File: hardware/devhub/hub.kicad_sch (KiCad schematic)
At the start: 34 parts, among them J2 USB-C UPSTREAM, J3 PORTA 7 (scorta), U12 MCP120T-300I/TT, U2 USB2517I-JZX, Y1 24MHz 12pF

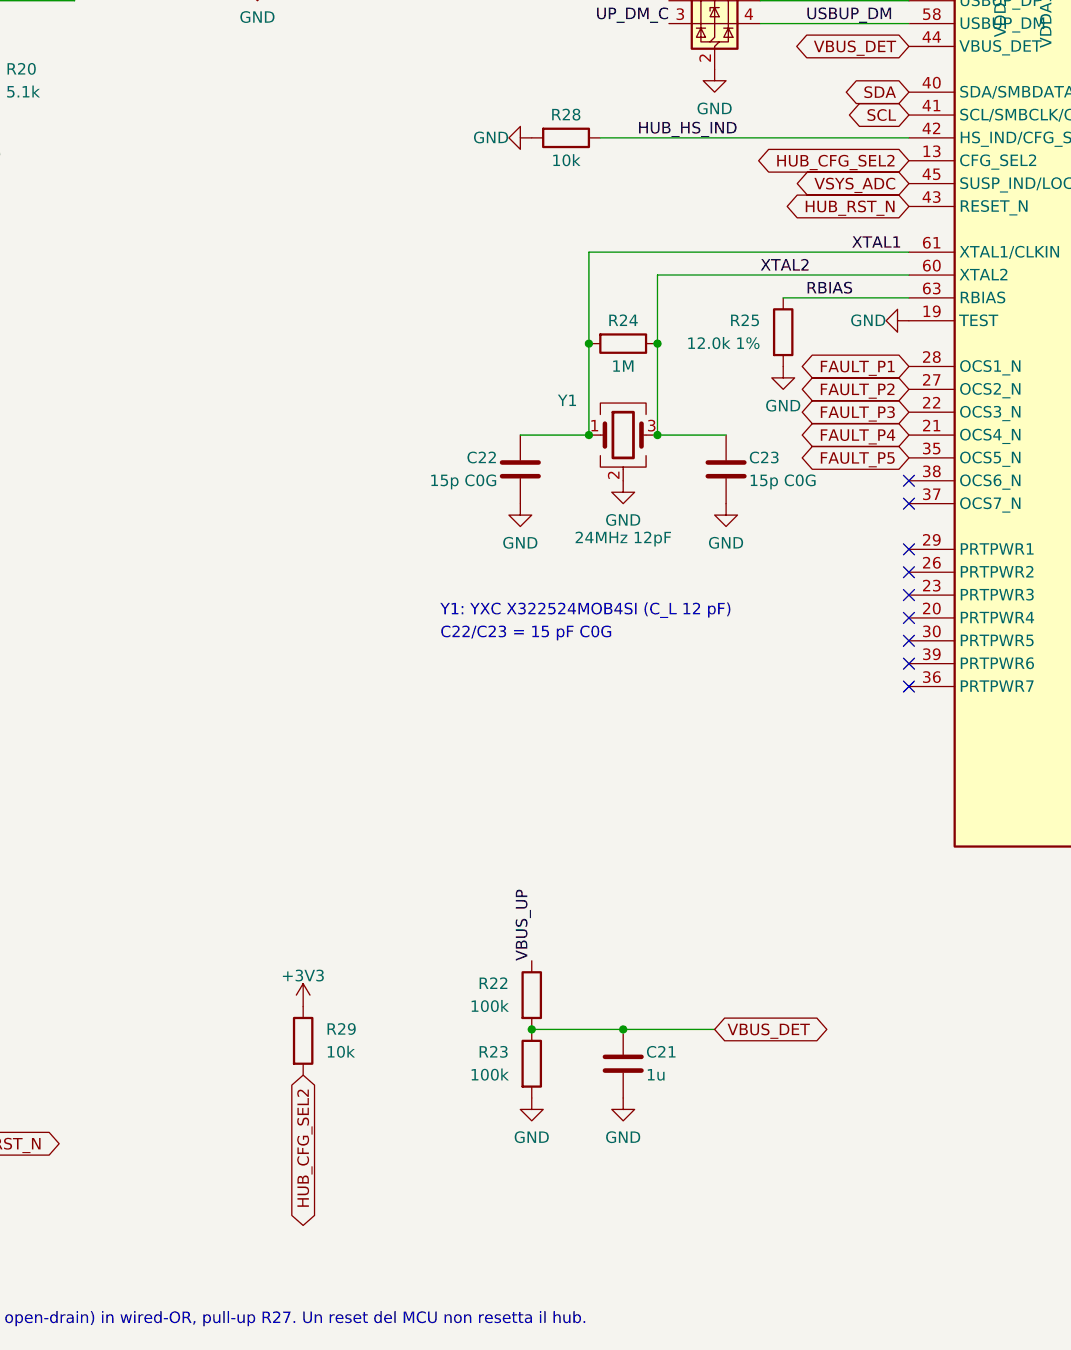
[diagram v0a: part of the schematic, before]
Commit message: Simplification: input shunt moved after the eFuse, VSYS_ADC divider removed (D40)
The INA3221 is no longer exposed to the supply voltage and reads 5V_SYS; LOCAL_PWR gets a 10k pull-up (R26). Push-button capacitors kept (D39).
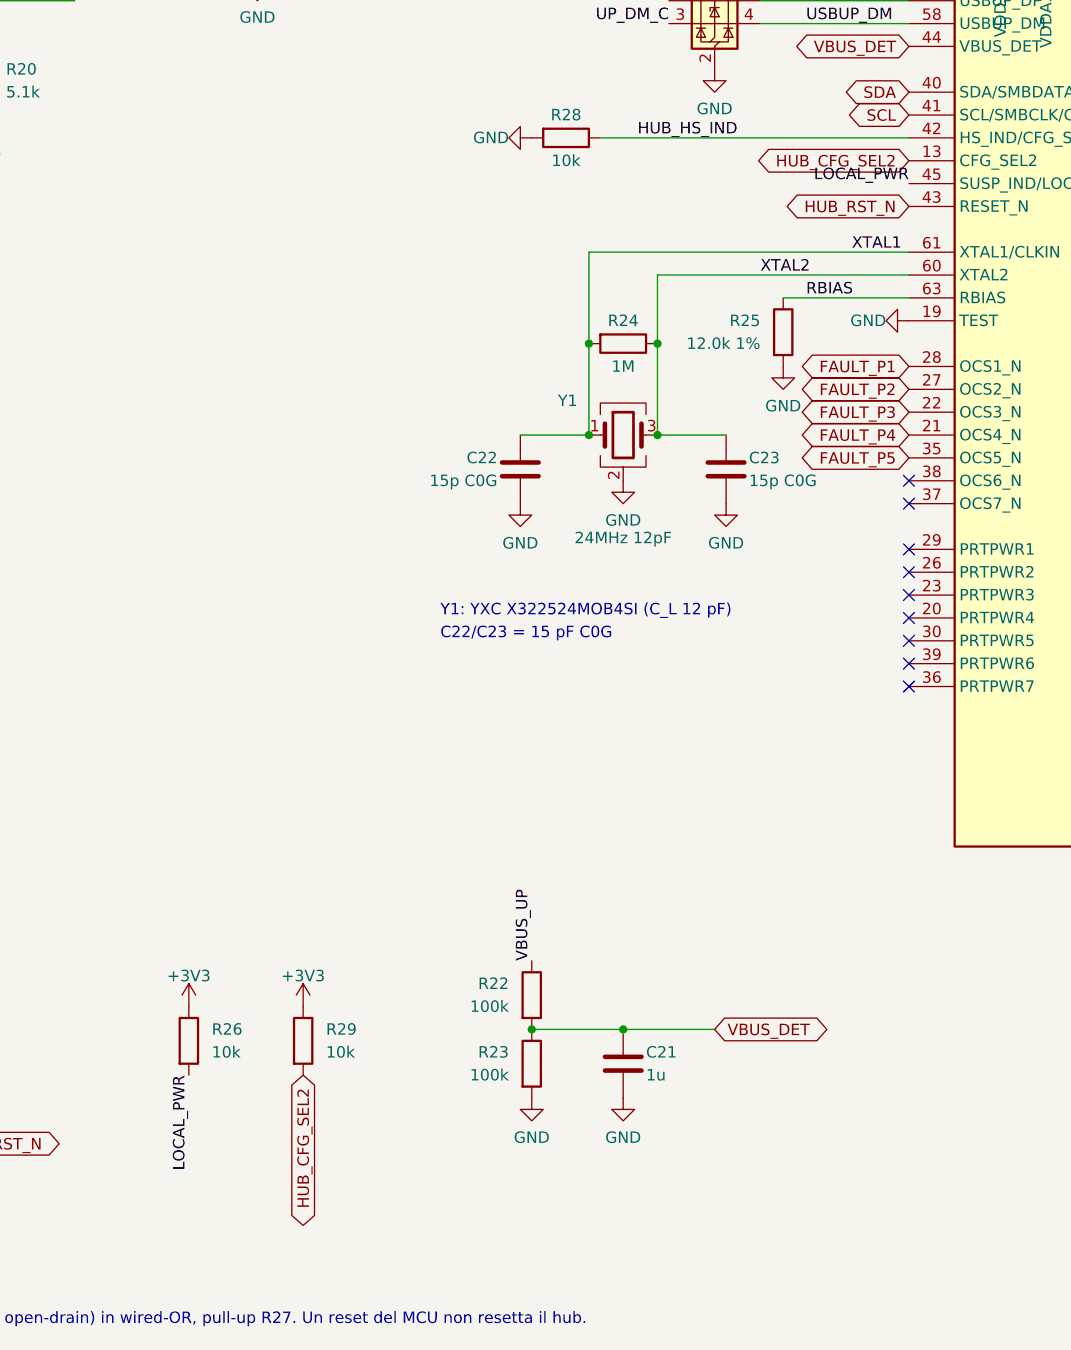
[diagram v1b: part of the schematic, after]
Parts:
- added R26: 10k, Resistor_SMD:R_0603_1608Metric, symbol Device:R
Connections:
- net +3V3: now also R26.1
- net VSYS_ADC renamed LOCAL_PWR
- net LOCAL_PWR: now also R26.2
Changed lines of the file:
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@@
 		)
 	)
+	(label "LOCAL_PWR"
+		(at 184.15 127 180)
+		(effects
+			(font
+				(size 1.27 1.27)
+			)
+			(justify right bottom)
+		)
+	)
+	(label "LOCAL_PWR"
+		(at 104.14 226.06 270)
+		(effects
+			(font
+				(size 1.27 1.27)
+			)
+			(justify right bottom)
+		)
+	)
 	(global_label "USB_MCU_DM"
 		(shape bidirectional)
@@
 		)
 	)
-	(global_label "VSYS_ADC"
-		(shape bidirectional)
-		(at 184.15 127 180)
-		(fields_autoplaced yes)
-		(effects
-			(font
-				(size 1.27 1.27)
-			)
-			(justify right)
-		)
-		(property "Intersheetrefs" "${INTERSHEET_REFS}"
-			(at 184.15 127 0)
-			(hide yes)
-			(show_name no)
-			(do_not_autoplace no)
-			(effects
-				(font
-					(size 1.27 1.27)
-				)
-			)
-		)
-	)
 	(symbol
 		(lib_id "Device:R")
@@
 					(unit 1)
 				)
+			)
+		)
+	)
+	(symbol
+		(lib_id "Device:R")
+		(at 104.14 222.25 0)
+		(unit 1)
+		(body_style 1)
+		(exclude_from_sim no)
+		(in_bom yes)
+		(on_board yes)
+		(in_pos_files yes)
+		(dnp no)
+		(property "Reference" "R26"
+			(at 106.68 220.98 0)
+			(show_name no)
+			(do_not_autoplace no)
+			(effects
+				(font
+					(size 1.27 1.27)
+				)
+				(justify left)
+			)
+		)
+		(property "Value" "10k"
+			(at 106.68 223.52 0)
+			(show_name no)
+			(do_not_autoplace no)
+			(effects
+				(font
+					(size 1.27 1.27)
+				)
+				(justify left)
+			)
+		)
+		(property "Footprint" "Resistor_SMD:R_0603_1608Metric"
+			(at 104.14 222.25 0)
+			(hide yes)
+			(show_name no)
+			(do_not_autoplace no)
+			(effects
+				(font
+					(size 1.27 1.27)
+				)
+			)
+		)
+		(property "Datasheet" ""
+			(at 104.14 222.25 0)
+			(hide yes)
+			(show_name no)
+			(do_not_autoplace no)
+			(effects
+				(font
+					(size 1.27 1.27)
+				)
+			)
+		)
+		(property "Description" "Resistor"
+			(at 104.14 222.25 0)
+			(hide yes)
+			(show_name no)
+			(do_not_autoplace no)
+			(effects
+				(font
+					(size 1.27 1.27)
+				)
+			)
+		)
+		(pin "1"
+		)
+		(pin "2"
+		)
+		(instances
+			(project "devhub"
+				(path "/af6ea7d8-d1ba-5fc6-aec8-abf514847630/af081a2b-4668-5eab-8d09-70b13e5ee477"
+					(reference "R26")
+					(unit 1)
+				)
+			)
+		)
+	)
+	(symbol
+		(lib_id "power:+3V3")
+		(at 104.14 218.44 0)
+		(unit 1)
+		(body_style 1)
+		(exclude_from_sim no)
+		(in_bom yes)
+		(on_board yes)
+		(in_pos_files yes)
+		(dnp no)
+		(property "Reference" "#PWR161"
+			(at 104.14 218.44 0)
+			(hide yes)
+			(show_name no)
+			(do_not_autoplace no)
+			(effects
+				(font
+					(size 1.27 1.27)
+				)
+			)
+		)
+		(property "Value" "+3V3"
+			(at 104.14 215.04 0)
+			(show_name no)
+			(do_not_autoplace no)
+			(effects
+				(font
+					(size 1.27 1.27)
+				)
+			)
+		)
+		(property "Footprint" ""
+			(at 104.14 218.44 0)
+			(hide yes)
+			(show_name no)
+			(do_not_autoplace no)
+			(effects
+				(font
+					(size 1.27 1.27)
+				)
+			)
+		)
+		(property "Datasheet" ""
+			(at 104.14 218.44 0)
+			(hide yes)
+			(show_name no)
+			(do_not_autoplace no)
+			(effects
+				(font
+					(size 1.27 1.27)
+				)
+			)
+		)
+		(property "Description" ""
+			(at 104.14 218.44 0)
+			(hide yes)
+			(show_name no)
+			(do_not_autoplace no)
+			(effects
+				(font
+					(size 1.27 1.27)
+				)
+			)
+		)
+		(pin "1"
+		)
+		(instances
+			(project "devhub"
+				(path "/af6ea7d8-d1ba-5fc6-aec8-abf514847630/af081a2b-4668-5eab-8d09-70b13e5ee477"
+					(reference "#PWR161")
+					(unit 1)
+				)

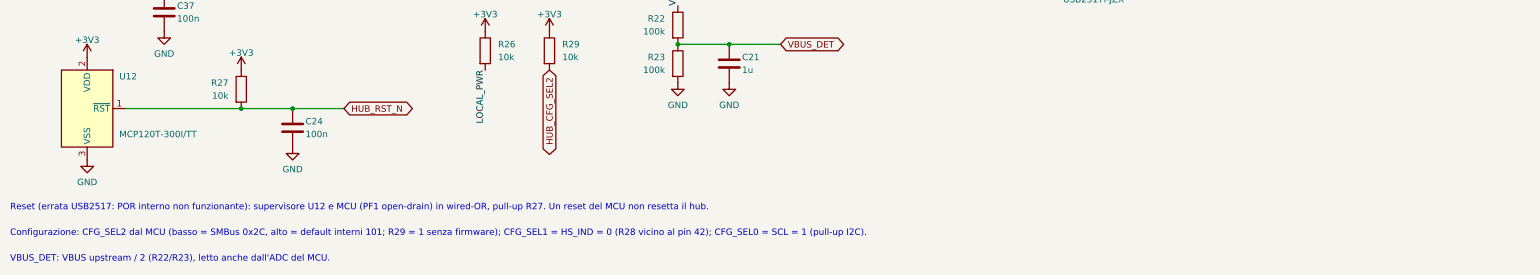
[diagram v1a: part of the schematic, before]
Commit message: Simplification: hub reset capacitor C24 set to DNP (D41)
The MCP120 generates the reset delay internally; the pad stays in case spurious hub resets show up.
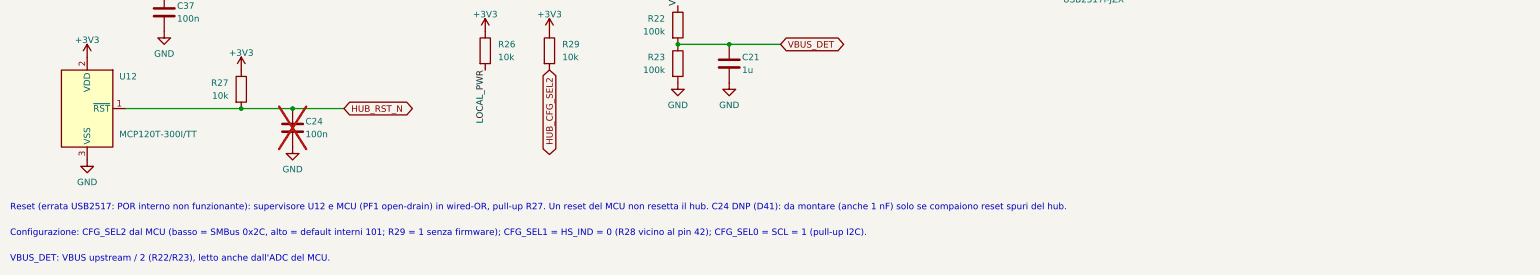
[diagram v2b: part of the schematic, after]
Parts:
- C24: now not fitted
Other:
- note added: "Reset (errata USB2517: POR interno non funzionante): supervisore U12 e MCU (PF1 open-drain) in wired-OR, pull-up R27. Un reset del MCU non resetta il hub. C24 DNP (D41): da montare (anche 1 nF) solo se compaiono reset spuri del hub."
- note removed: "Reset (errata USB2517: POR interno non funzionante): supervisore U12 e MCU (PF1 open-drain) in wired-OR, pull-up R27. Un reset del MCU non resetta il hub."
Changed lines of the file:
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@@
 		)
 	)
-	(text "Reset (errata USB2517: POR interno non funzionante): supervisore U12 e MCU (PF1 open-drain) in wired-OR, pull-up R27. Un reset del MCU non resetta il hub."
+	(text "Reset (errata USB2517: POR interno non funzionante): supervisore U12 e MCU (PF1 open-drain) in wired-OR, pull-up R27. Un reset del MCU non resetta il hub. C24 DNP (D41): da montare (anche 1 nF) solo se compaiono reset spuri del hub."
 		(exclude_from_sim no)
 		(at 10.16 254 0)
@@
 		(on_board yes)
 		(in_pos_files yes)
-		(dnp no)
+		(dnp yes)
 		(property "Reference" "C24"
 			(at 68.58 236.22 0)

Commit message: PCB rules in KiCad, USB pair names, eFuse output bypass and U2 thermal vias (D44-D50)
Stackup JLC04161H-7628, netclasses and custom DRC rules (devhub.kicad_dru) from
docs/regole-pcb.md, with a section for the checks that DRC cannot cover. C7 1 uF on
the TPS259470A output before the shunt (D48). USB nets renamed to DP/DN so KiCad
recognizes the differential pairs (D49). U2 footprint with 0.3 mm thermal vias, open
on both sides for the prototype; encroached vias and a JLCPCB order note for
production (D50). Also includes stock part codes, cost comparison and placement rules
(D44-D47).
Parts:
- C20: digikey (none) -> 1276-1065-1-ND; lcsc (none) -> C1746; mouser (none) -> 187-CL21A475KOFNNNE; warehouse (none) -> 236
- C21, C31, C32, C33, C35: digikey (none) -> 1276-1184-1-ND; lcsc (none) -> C29936; mouser (none) -> 187-CL10B105KA8NNNC; warehouse (none) -> 240
- C22, C23: digikey (none) -> 1276-1296-1-ND; lcsc (none) -> C1644; mouser (none) -> 187-CL10C150JB8NNNC
- C24, C25, C26, C27, C28, C29, C30, C34, C36, C37: digikey (none) -> 1276-1000-1-ND; lcsc (none) -> C1591; mouser (none) -> 187-CL10B104KB8NNNC; warehouse (none) -> 235
- D20: digikey (none) -> 497-5235-1-ND; lcsc (none) -> C7519; mouser (none) -> 511-USBLC6-2SC6; warehouse (none) -> 277
- F1: footprint Fuse:Fuse_1206_3216Metric -> Fuse:Fuse_1812_4532Metric; digikey (none) -> MF-MSMF050-2CT-ND; lcsc (none) -> C17313; mouser (none) -> 652-MF-MSMF050-2; warehouse (none) -> 210
- J2: digikey (none) -> 2073-USB4105-GF-ACT-ND; lcsc (none) -> C3020560; mouser (none) -> 640-USB4105-GF-A; warehouse (none) -> 279
- J3: digikey (none) -> 732-5317-ND; lcsc (none) -> C124378; mouser (none) -> 710-61300411121
- R20, R21: digikey (none) -> 311-5.10KHRCT-ND; lcsc (none) -> C23186; mouser (none) -> 603-RC0603FR-075K1L; warehouse (none) -> 238
- R22, R23: digikey (none) -> 311-100KHRCT-ND; lcsc (none) -> C2906980; mouser (none) -> 603-RC0603FR-07100KL; warehouse (none) -> 247
- R24: digikey (none) -> 311-1.00MHRCT-ND; lcsc (none) -> C2907003; mouser (none) -> 603-RC0603FR-071ML; warehouse (none) -> 249
- R25: digikey (none) -> 311-12.0KHRCT-ND; lcsc (none) -> C114659; mouser (none) -> 603-RC0603FR-0712KL
- R26, R27, R28, R29: digikey (none) -> 311-10.0KHRCT-ND; lcsc (none) -> C2906982; mouser (none) -> 603-RC0603FR-0710KL; warehouse (none) -> 248
- U12: digikey (none) -> MCP120T-300I/TTCT-ND; lcsc (none) -> C625180; mouser (none) -> 579-MCP120T-300I/TT
- U2: footprint Package_DFN_QFN:QFN-64-1EP_9x9mm_P0.5mm_EP4.7x4.7mm_ThermalVias -> lcsc_footprints:QFN-64-1EP_9x9mm_P0.5mm_EP4.7x4.7mm_ThermalVias_0.3mm; digikey (none) -> 638-1090-ND; lcsc (none) -> C478081; mouser (none) -> 886-USB2517I-JZX
- Y1: digikey (none) -> XC2150CT-ND; lcsc (none) -> C70590; mouser (none) -> 520-240-12-33Q-JEST
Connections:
- net HUB_DM1 renamed HUB_DN1
- net HUB_DM2 renamed HUB_DN2
- net HUB_DM3 renamed HUB_DN3
- net HUB_DM4 renamed HUB_DN4
- net HUB_DM5 renamed HUB_DN5
- net SPARE_DM renamed SPARE_DN
- net UP_DM_C renamed UP_CONN_DN
- net UP_DP_C renamed UP_CONN_DP
- net USBUP_DM renamed USBUP_DN
- net USB_MCU_DM renamed USB_MCU_DN

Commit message: Review 03 fixes and PCB placement update (D51-D56)
Schematic review 03 (docs/lavorazioni/review_03.md):
- D1 SMAJ20A was reversed (cathode on GND): rotated, and replaced by a project
  symbol devhub:SMAJ20A with explicit K/A pin names; breakdown corrected to
  22.2-24.5 V (R03-01).
- D21 BAT54WS from VBUS_DET to 3V3 keeps USB2517 pin 44 within VDD33 + 0.5 V
  when the hub is unpowered (D53, R03-02).
- USB-A port limited to 1.5 A, the J501 connector rating: R62 33.2k, RF-5
  updated (D54, R03-03).
- RF-6 accuracy relaxed to 2 mA + 5 % because of the thick-film shunt TCR
  (D55, R03-04).
- Courtyards of the LCSC U13 and PI3USB4002A footprints enlarged to cover the
  pads, also in the PCB copies (R03-05).
- LDO U1 kept (buck rejected); GND heatsink zone and 10 vias on its tab, thermal
  budget corrected to 0.8-0.9 W worst case (D56).

PCB: connector layout (D51), USB pair polarity on the bottom side (D52), relays
moved with the contact keepout areas redrawn, D21 placed next to C21. Cost
comparison updated with D21 and R62.
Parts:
- added D21: BAT54WS, Diode_SMD:D_SOD-323, symbol Device:D_Schottky
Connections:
- net +3V3: now also D21.1 (K)
- net UP_CONN_DN: now also D20.1 (I/O1); no longer D20.3 (I/O2)
- net UP_CONN_DP: now also D20.3 (I/O2); no longer D20.1 (I/O1)
- net USBUP_DN: now also D20.6 (I/O1); no longer D20.4 (I/O2)
- net USBUP_DP: now also D20.4 (I/O2); no longer D20.6 (I/O1)
- net VBUS_DET: now also D21.2 (A)
